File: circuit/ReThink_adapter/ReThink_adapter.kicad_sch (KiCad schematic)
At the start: 78 parts, among them J1 FH34SRJ-34S-0.5SH(50), J10 OUT2, J11 OUT3, J2 FH34SRJ-6S-0.5SH(50), J3 Mezzanine, J4 XF3M(1)-3015-1B, J5 XF3M(1)-0815-1B, J6 FH34SRJ-40S-0.5SH(50), J7 FH52-40S-0.5SH, J8 XF3M(1)-1415-1B, J9 OUT1, U1 PCAL6416AHF, U2 LM2775DSG, U3 PCA9306, U4 TPS610333DRLR

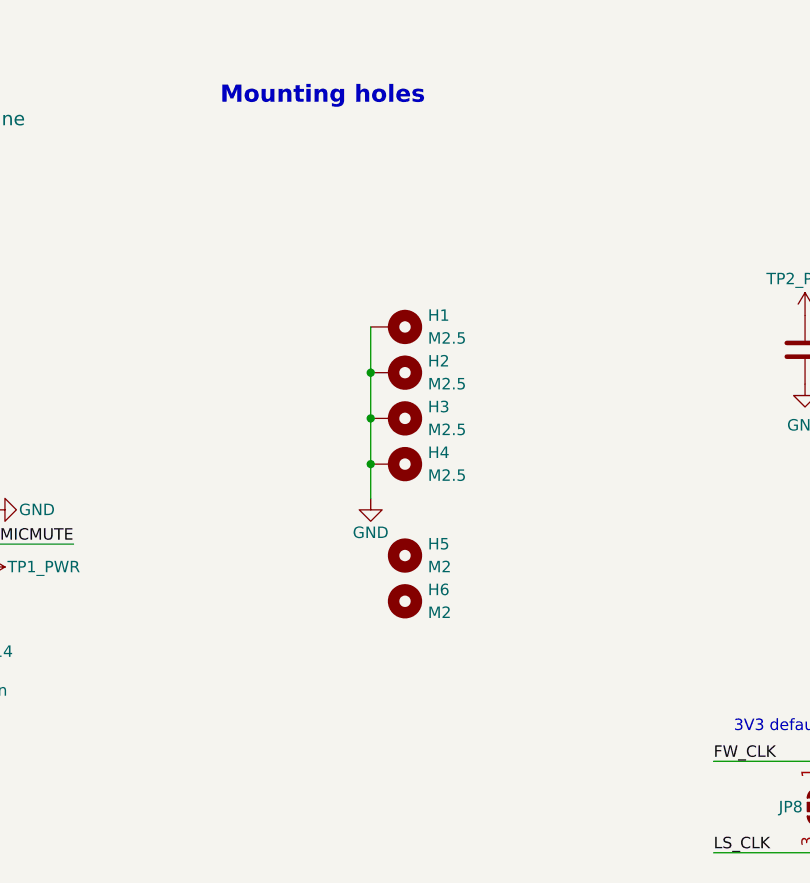
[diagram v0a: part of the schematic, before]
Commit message: Added connector guide, start adding keyboard mounting holes
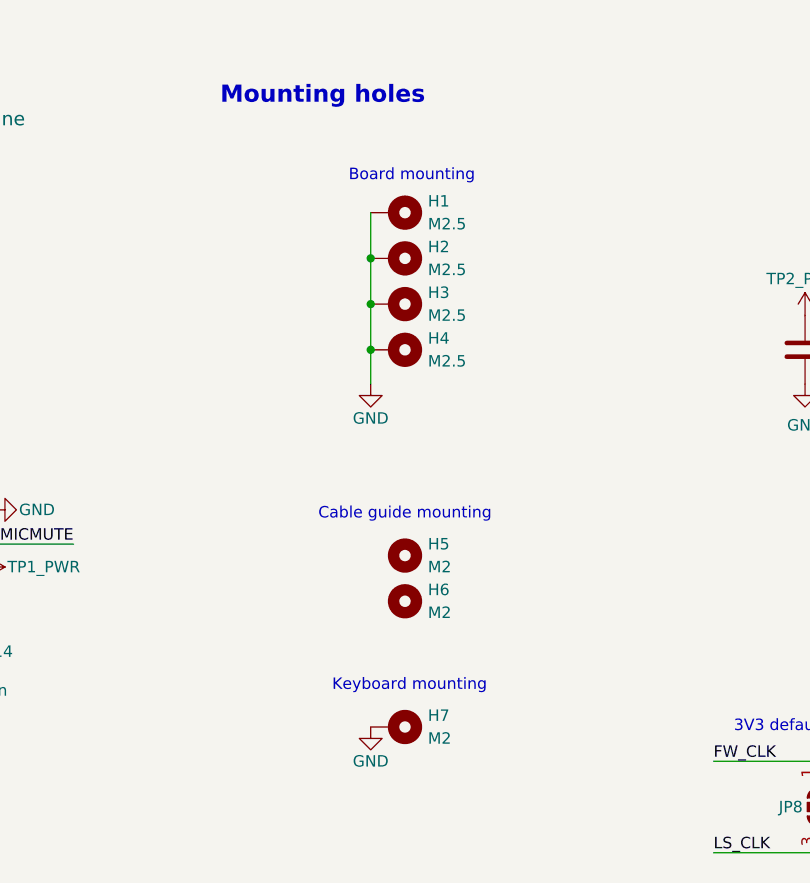
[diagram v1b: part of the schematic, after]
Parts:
- added H7: M2, MountingHole:MountingHole_2.2mm_M2_ISO14580_Pad, symbol Mechanical:MountingHole_Pad
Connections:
- net GND: now also H7.1
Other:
- note added: "Board mounting"
- note added: "Cable guide mounting"
- note added: "Keyboard mounting"
- moved on the sheet: H1, H2, H3, H4

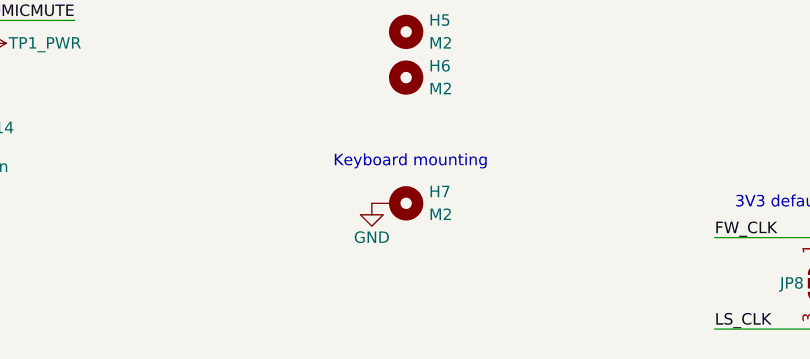
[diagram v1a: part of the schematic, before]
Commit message: add keyboard mounting holes
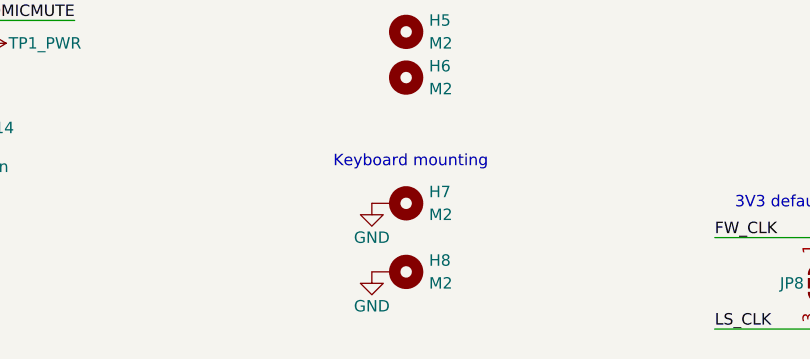
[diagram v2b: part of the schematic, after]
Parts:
- added H8: M2, MountingHole:MountingHole_2.2mm_M2_ISO14580_Pad, symbol Mechanical:MountingHole_Pad
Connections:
- net GND: now also H8.1
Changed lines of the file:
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@@
 	)
 	(symbol
+		(lib_id "Mechanical:MountingHole_Pad")
+		(at 156.21 257.81 270)
+		(unit 1)
+		(body_style 1)
+		(exclude_from_sim no)
+		(in_bom no)
+		(on_board yes)
+		(in_pos_files yes)
+		(dnp no)
+		(fields_autoplaced yes)
+		(property "Reference" "H8"
+			(at 160.02 256.5399 90)
+			(show_name no)
+			(do_not_autoplace no)
+			(effects
+				(font
+					(size 1.27 1.27)
+				)
+				(justify left)
+			)
+		)
+		(property "Value" "M2"
+			(at 160.02 259.0799 90)
+			(show_name no)
+			(do_not_autoplace no)
+			(effects
+				(font
+					(size 1.27 1.27)
+				)
+				(justify left)
+			)
+		)
+		(property "Footprint" "MountingHole:MountingHole_2.2mm_M2_ISO14580_Pad"
+			(at 156.21 257.81 0)
+			(hide yes)
+			(show_name no)
+			(do_not_autoplace no)
+			(effects
+				(font
+					(size 1.27 1.27)
+				)
+			)
+		)
+		(property "Datasheet" ""
+			(at 156.21 257.81 0)
+			(hide yes)
+			(show_name no)
+			(do_not_autoplace no)
+			(effects
+				(font
+					(size 1.27 1.27)
+				)
+			)
+		)
+		(property "Description" "Mounting Hole with connection"
+			(at 156.21 257.81 0)
+			(hide yes)
+			(show_name no)
+			(do_not_autoplace no)
+			(effects
+				(font
+					(size 1.27 1.27)
+				)
+			)
+		)
+		(pin "1"
+		)
+		(instances
+			(project "ReThink_adapter"
+				(path "/6cef7f30-4344-4878-be02-7aa54a02ef81"
+					(reference "H8")
+					(unit 1)
+				)
+			)
+		)
+	)
+	(symbol
 		(lib_id "power:GND")
 		(at 45.72 142.24 90)
@@
 					(unit 1)
 				)
+			)
+		)
+	)
+	(symbol
+		(lib_id "power:GND")
+		(at 153.67 257.81 0)
+		(mirror y)
+		(unit 1)
+		(body_style 1)
+		(exclude_from_sim no)
+		(in_bom yes)
+		(on_board yes)
+		(in_pos_files yes)
+		(dnp no)
+		(property "Reference" "#PWR088"
+			(at 153.67 264.16 0)
+			(hide yes)
+			(show_name no)
+			(do_not_autoplace no)
+			(effects
+				(font
+					(size 1.27 1.27)
+				)
+			)
+		)
+		(property "Value" "GND"
+			(at 153.67 261.62 0)
+			(show_name no)
+			(do_not_autoplace no)
+			(effects
+				(font
+					(size 1.27 1.27)
+				)
+			)
+		)
+		(property "Footprint" ""
+			(at 153.67 257.81 0)
+			(hide yes)
+			(show_name no)
+			(do_not_autoplace no)
+			(effects
+				(font
+					(size 1.27 1.27)
+				)
+			)
+		)
+		(property "Datasheet" ""
+			(at 153.67 257.81 0)
+			(hide yes)
+			(show_name no)
+			(do_not_autoplace no)
+			(effects
+				(font
+					(size 1.27 1.27)
+				)
+			)
+		)
+		(property "Description" "Power symbol creates a global label with name \"GND\" , ground"
+			(at 153.67 257.81 0)
+			(hide yes)
+			(show_name no)
+			(do_not_autoplace no)
+			(effects
+				(font
+					(size 1.27 1.27)
+				)
+			)
+		)
+		(pin "1"
+		)
+		(instances
+			(project "ReThink_adapter"
+				(path "/6cef7f30-4344-4878-be02-7aa54a02ef81"
+					(reference "#PWR088")
+					(unit 1)
+				)

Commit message: updated 3D models
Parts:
- C12, C13, C19, C20: Alt_MPN (none) -> 81-GRM219R61C226ME1K; Distributor link https://www.mouser.pl/en/ProductDetail/Murata-Electronics/G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 -> https://www.mouser.pl/en/ProductDetail/Samsung-Electro-Mech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; Mouser_PN 81-GRM219R61C226ME1K -> 187-CL21A226KOQNNNG
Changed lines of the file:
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@@
 			)
 		)
-		(property "Distributor link" "https://www.mouser.pl/en/ProductDetail/Murata-Electronics/GRM219R61C226ME15K?qs=F5EMLAvA7IDHNVqFg3MF1Q%3D%3D"
+		(property "Distributor link" "https://www.mouser.pl/en/ProductDetail/Samsung-Electro-Mechanics/CL21A226KOQNNNG?qs=y02iAgv9n63ATGKnSfEDrg%3D%3D"
 			(at 39.37 226.06 0)
 			(hide yes)
@@
 			)
 		)
-		(property "Alt_MPN" ""
+		(property "Alt_MPN" "81-GRM219R61C226ME1K"
 			(at 39.37 226.06 0)
 			(hide yes)
@@
 			)
 		)
-		(property "Mouser_PN" "81-GRM219R61C226ME1K"
+		(property "Mouser_PN" "187-CL21A226KOQNNNG"
 			(at 39.37 226.06 0)
 			(hide yes)
@@
 			)
 		)
-		(property "Distributor link" "https://www.mouser.pl/en/ProductDetail/Murata-Electronics/GRM219R61C226ME15K?qs=F5EMLAvA7IDHNVqFg3MF1Q%3D%3D"
+		(property "Distributor link" "https://www.mouser.pl/en/ProductDetail/Samsung-Electro-Mechanics/CL21A226KOQNNNG?qs=y02iAgv9n63ATGKnSfEDrg%3D%3D"
 			(at 217.17 218.44 0)
 			(hide yes)
@@
 			)
 		)
-		(property "Alt_MPN" ""
+		(property "Alt_MPN" "81-GRM219R61C226ME1K"
 			(at 217.17 218.44 0)
 			(hide yes)
@@
 			)
 		)
-		(property "Mouser_PN" "81-GRM219R61C226ME1K"
+		(property "Mouser_PN" "187-CL21A226KOQNNNG"
 			(at 217.17 218.44 0)
 			(hide yes)
@@
 			)
 		)
-		(property "Distributor link" "https://www.mouser.pl/en/ProductDetail/Murata-Electronics/GRM219R61C226ME15K?qs=F5EMLAvA7IDHNVqFg3MF1Q%3D%3D"
+		(property "Distributor link" "https://www.mouser.pl/en/ProductDetail/Samsung-Electro-Mechanics/CL21A226KOQNNNG?qs=y02iAgv9n63ATGKnSfEDrg%3D%3D"
 			(at 31.75 226.06 0)
 			(hide yes)
@@
 			)
 		)
-		(property "Alt_MPN" ""
+		(property "Alt_MPN" "81-GRM219R61C226ME1K"
 			(at 31.75 226.06 0)
 			(hide yes)
@@
 			)
 		)
-		(property "Mouser_PN" "81-GRM219R61C226ME1K"
+		(property "Mouser_PN" "187-CL21A226KOQNNNG"
 			(at 31.75 226.06 0)
 			(hide yes)
@@
 			)
 		)
-		(property "Distributor link" "https://www.mouser.pl/en/ProductDetail/Murata-Electronics/GRM219R61C226ME15K?qs=F5EMLAvA7IDHNVqFg3MF1Q%3D%3D"
+		(property "Distributor link" "https://www.mouser.pl/en/ProductDetail/Samsung-Electro-Mechanics/CL21A226KOQNNNG?qs=y02iAgv9n63ATGKnSfEDrg%3D%3D"
 			(at 224.79 218.44 0)
 			(hide yes)
@@
 			)
 		)
-		(property "Alt_MPN" ""
+		(property "Alt_MPN" "81-GRM219R61C226ME1K"
 			(at 224.79 218.44 0)
 			(hide yes)
@@
 			)
 		)
-		(property "Mouser_PN" "81-GRM219R61C226ME1K"
+		(property "Mouser_PN" "187-CL21A226KOQNNNG"
 			(at 224.79 218.44 0)
 			(hide yes)

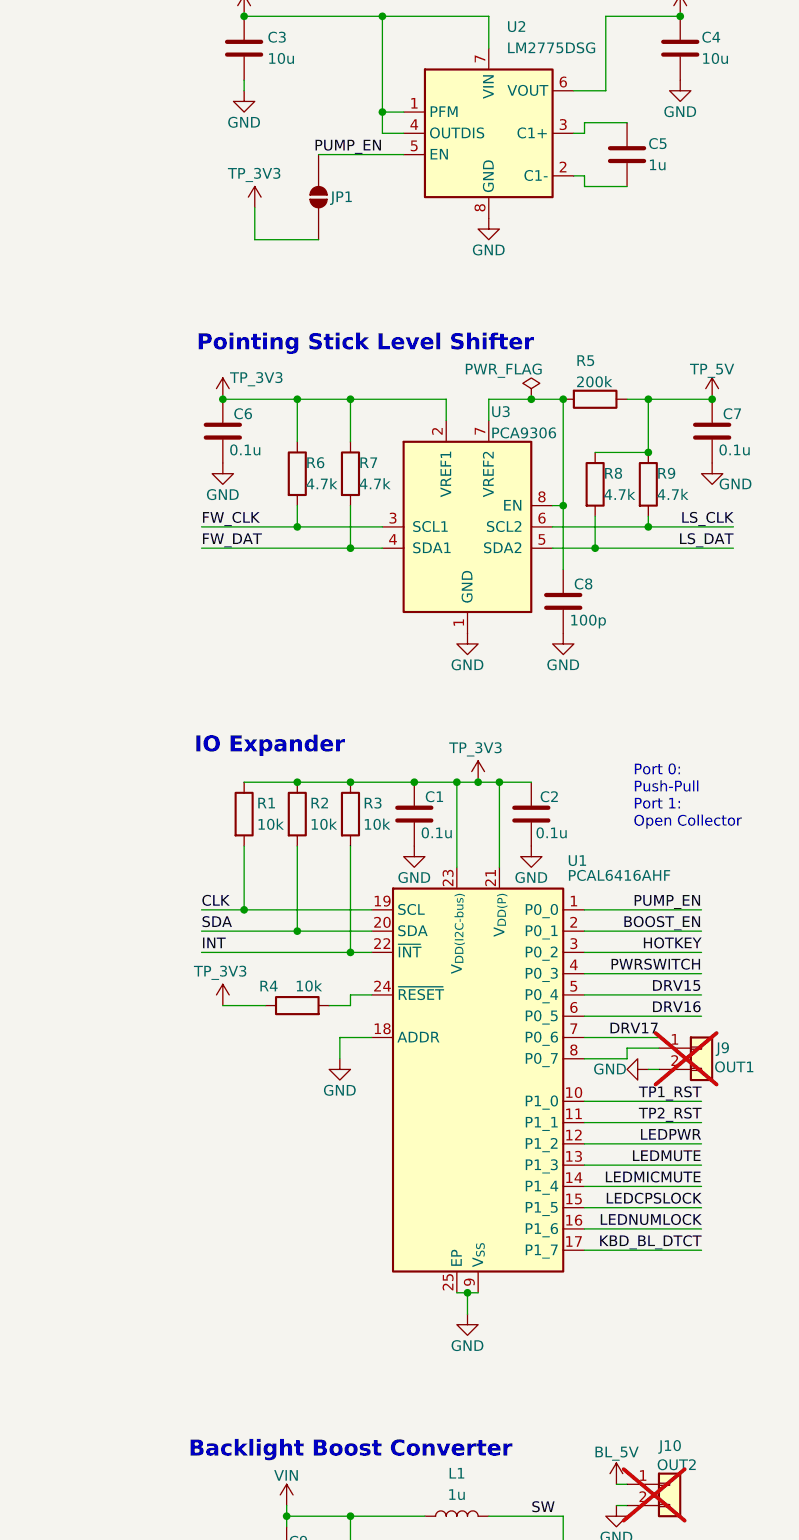
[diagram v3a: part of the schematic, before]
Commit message: add IO expander power selection jumper, charge pump enable pulldown
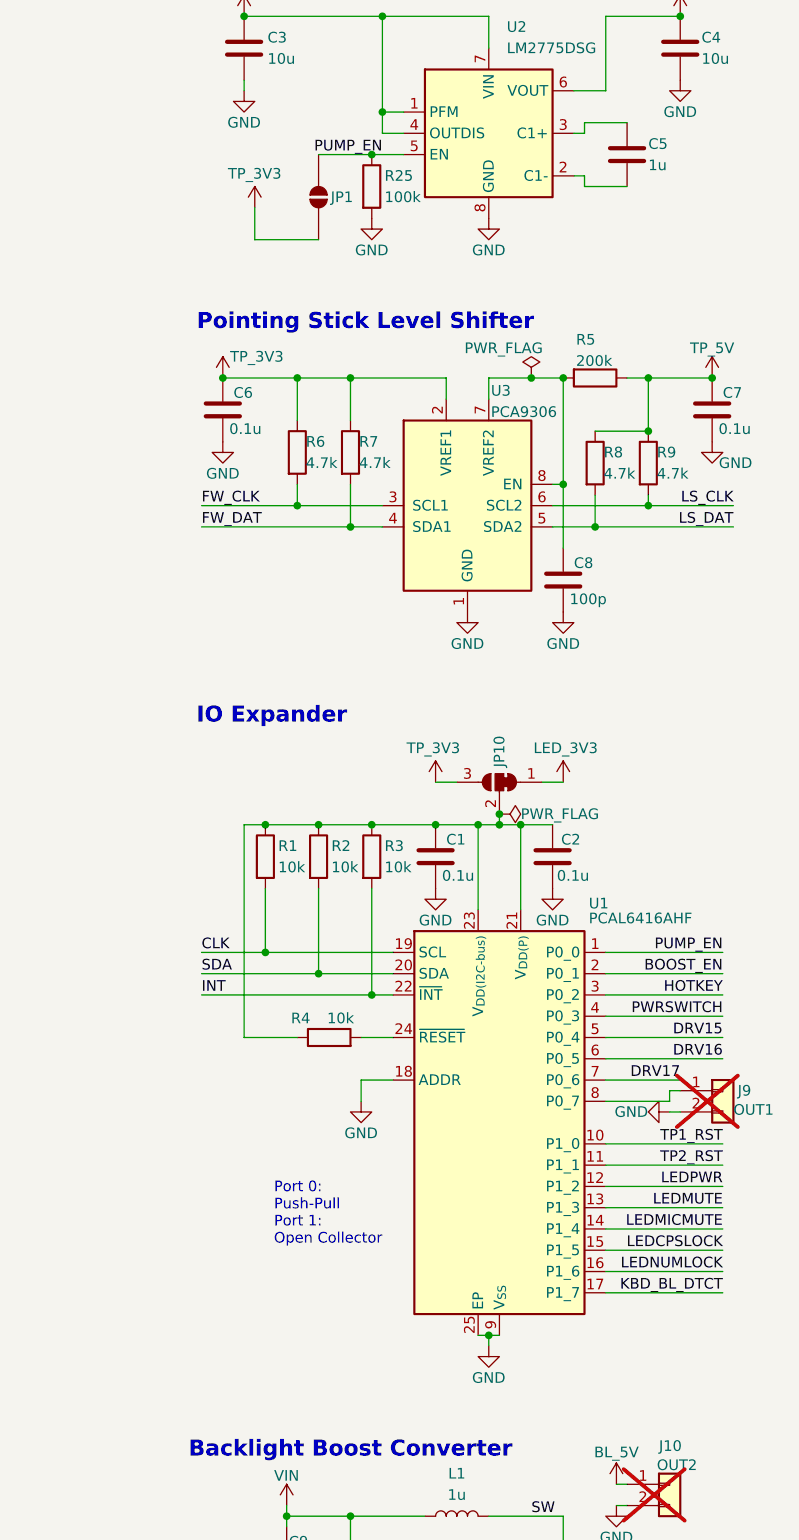
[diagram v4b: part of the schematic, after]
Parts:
- added JP10: SolderJumper_3_Bridged12, Jumper:SolderJumper-3_P1.3mm_Bridged12_RoundedPad1.0x1.5mm_NumberLabels, symbol Jumper:SolderJumper_3_Bridged12
- added R25: 100k, Resistor_SMD:R_0402_1005Metric, symbol Device:R
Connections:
- net GND: now also R25.2
- net LED_3V3: now also JP10.1 (A)
- net PUMP_EN: now also R25.1
- net TP_3V3: now also JP10.3 (B); no longer C1.1, C2.1, R1.1, R2.1, R3.1, R4.1, U1.21 (V_{DD(P)}), U1.23 (V_{DD(I2C-bus)})
- new net: C1.1, C2.1, JP10.2 (C), R1.1, R2.1, R3.1, R4.1, U1.21 (V_{DD(P)}), U1.23 (V_{DD(I2C-bus)})
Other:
- moved on the sheet: C1, C2, C6, C7, C8, J9, R1, R2, R3, R4, R5, R6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

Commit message: Add logo to readme, fix comments on schematic, add io expander pinout
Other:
- note added: "Warning! Short JP3 only for T430 backlight"
- note removed: "Port 0: Push-Pull Port 1: Open Collector"
- note removed: "Warning! Short JP2 only for T430 backlight"
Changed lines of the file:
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@@
 		)
 	)
-	(text "Warning! \nShort JP2 only \nfor T430 \nbacklight"
+	(text "Warning! \nShort JP3 only \nfor T430 \nbacklight"
 		(exclude_from_sim no)
 		(at 40.64 210.312 0)
@@
 		)
 	)
-	(text "Port 0:\nPush-Pull\nPort 1:\nOpen Collector"
-		(exclude_from_sim no)
-		(at 314.706 177.292 0)
-		(effects
-			(font
-				(size 1.27 1.27)
-			)
-			(justify left)
-		)
-	)
